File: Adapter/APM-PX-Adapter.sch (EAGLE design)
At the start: 13 parts, among them Q1 BSS138, Q2 BSS138

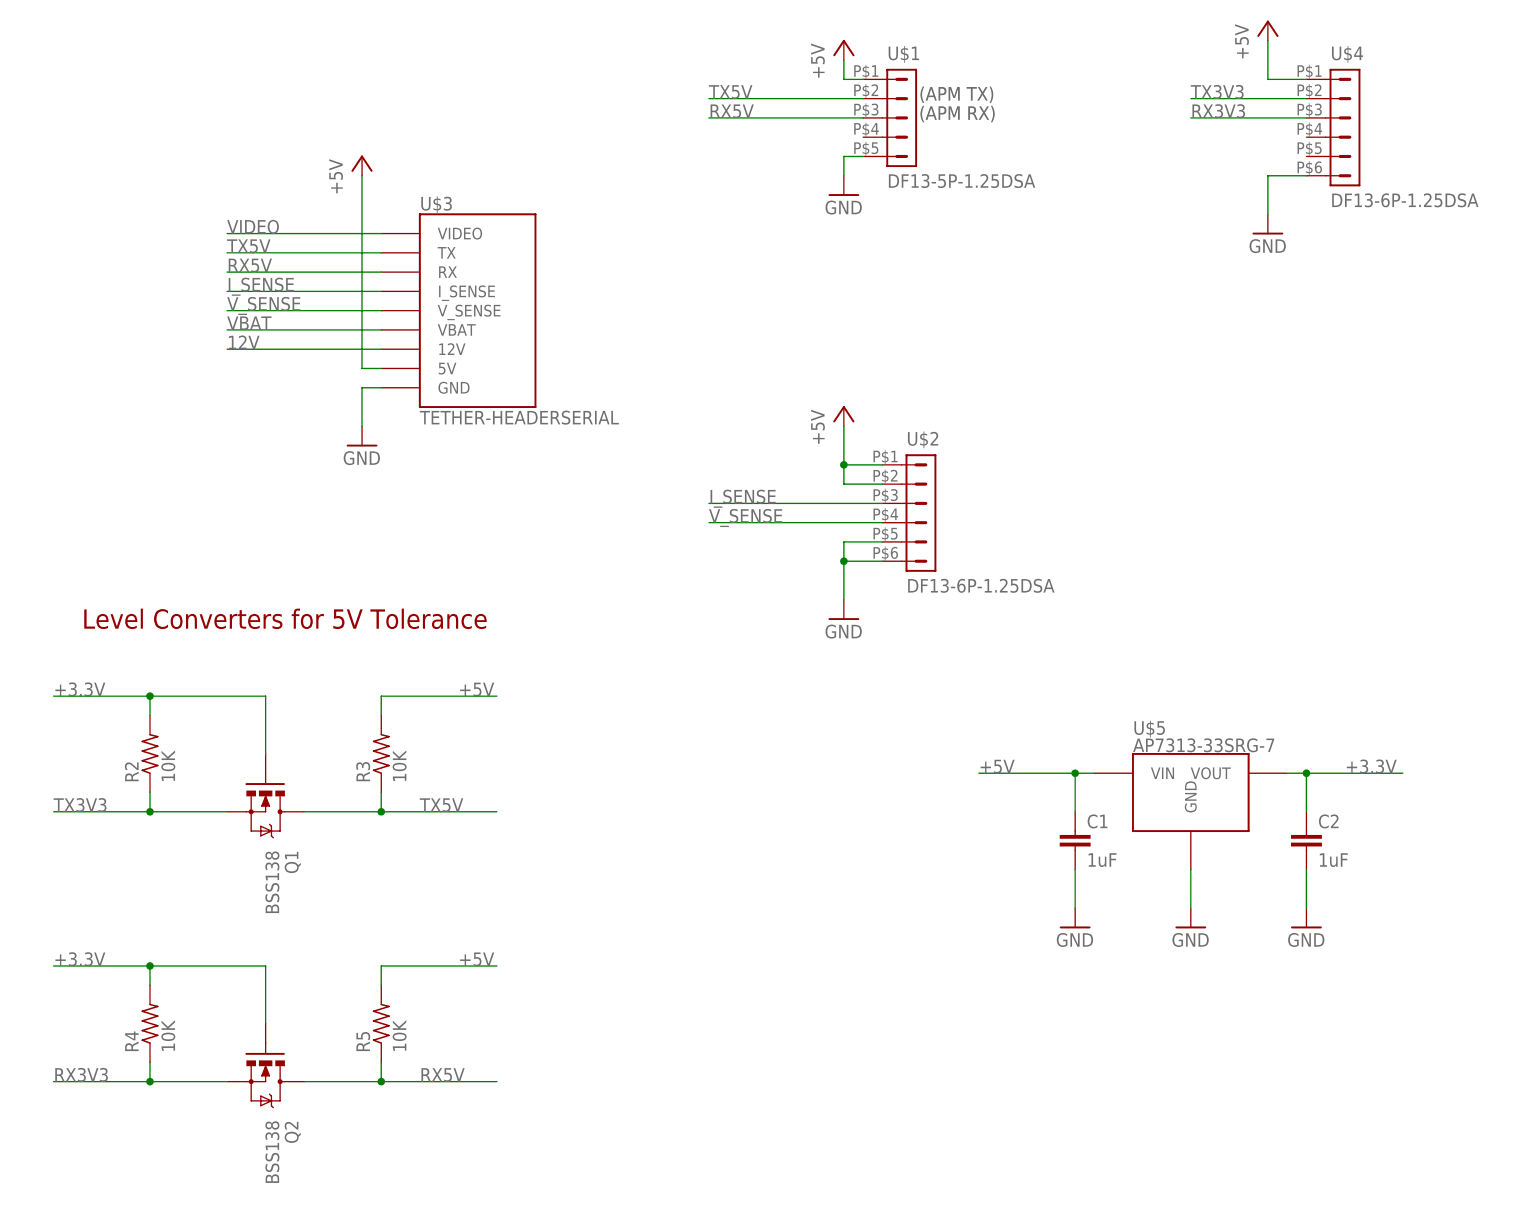
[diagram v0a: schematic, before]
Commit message: Removed level shifting and switch to all through hole components. Ordering a prototype.
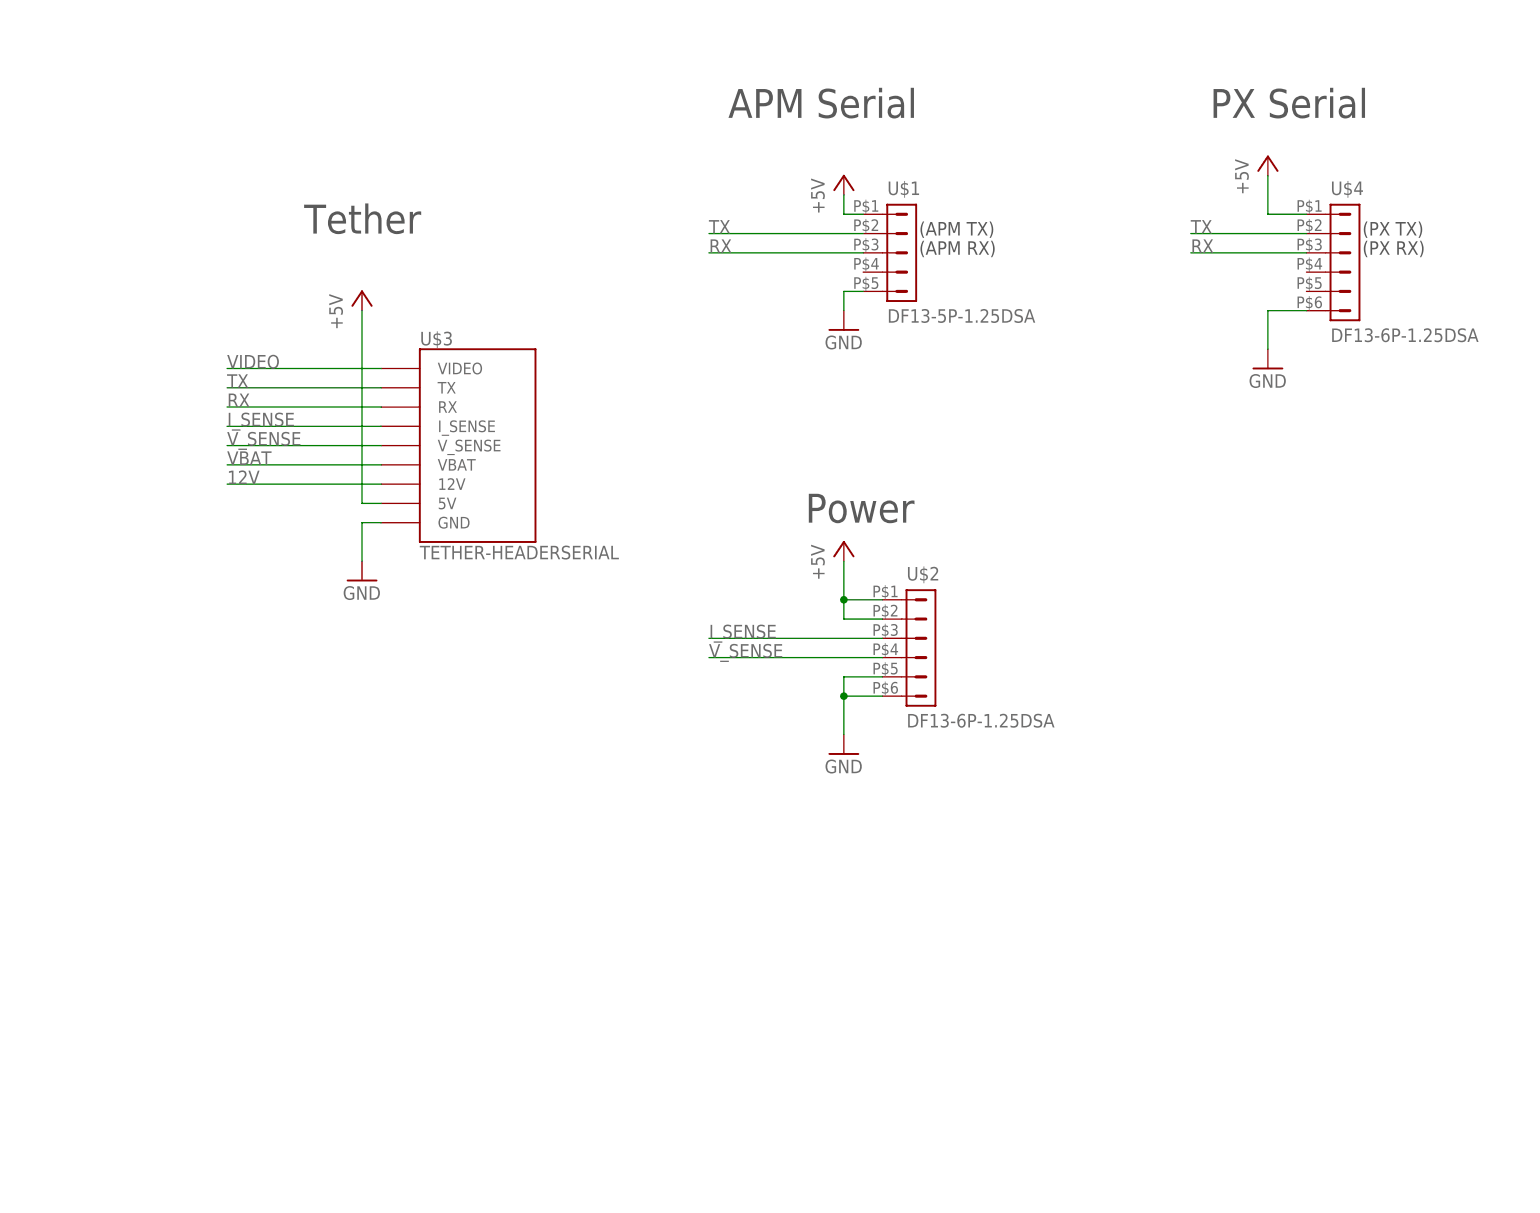
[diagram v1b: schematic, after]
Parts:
- removed C1, C2: 1uF, resistor:C-EUC0603
- removed Q1, Q2: BSS138, SparkFun-DiscreteSemi:MOSFET-NCHANNEL2N7002PW
- removed R2, R3, R4, R5: 10K, resistor:R-US_R0402
- removed U$5: AP7313-33SRG-7, BlueRobotics-Main:VREG-ZXTR2105
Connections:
- removed net +3.3V: C2.1, Q1.G, Q2.G, R2.2, R4.2, U$5.VOUT
- removed net RX3V3: Q2.S, R4.1, U$4.3
- removed net RX5V: Q2.D, R5.1, U$1.3, U$3.RX
- removed net TX3V3: Q1.S, R2.1, U$4.2
- removed net TX5V: Q1.D, R3.1, U$1.2, U$3.TX
- new net RX: U$1.3, U$3.RX, U$4.3
- new net TX: U$1.2, U$3.TX, U$4.2
- net +5V: no longer C1.1, R3.2, R5.2, U$5.VIN
- net GND: no longer C1.2, C2.2, U$5.GND
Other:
- note added: "(PX RX)"
- note added: "(PX TX)"
- note added: "APM Serial"
- note added: "PX Serial"
- note added: "Power"
- note added: "Tether"
- note removed: "Level Converters for 5V Tolerance"
- moved on the sheet: U$1, U$2, U$3, U$4

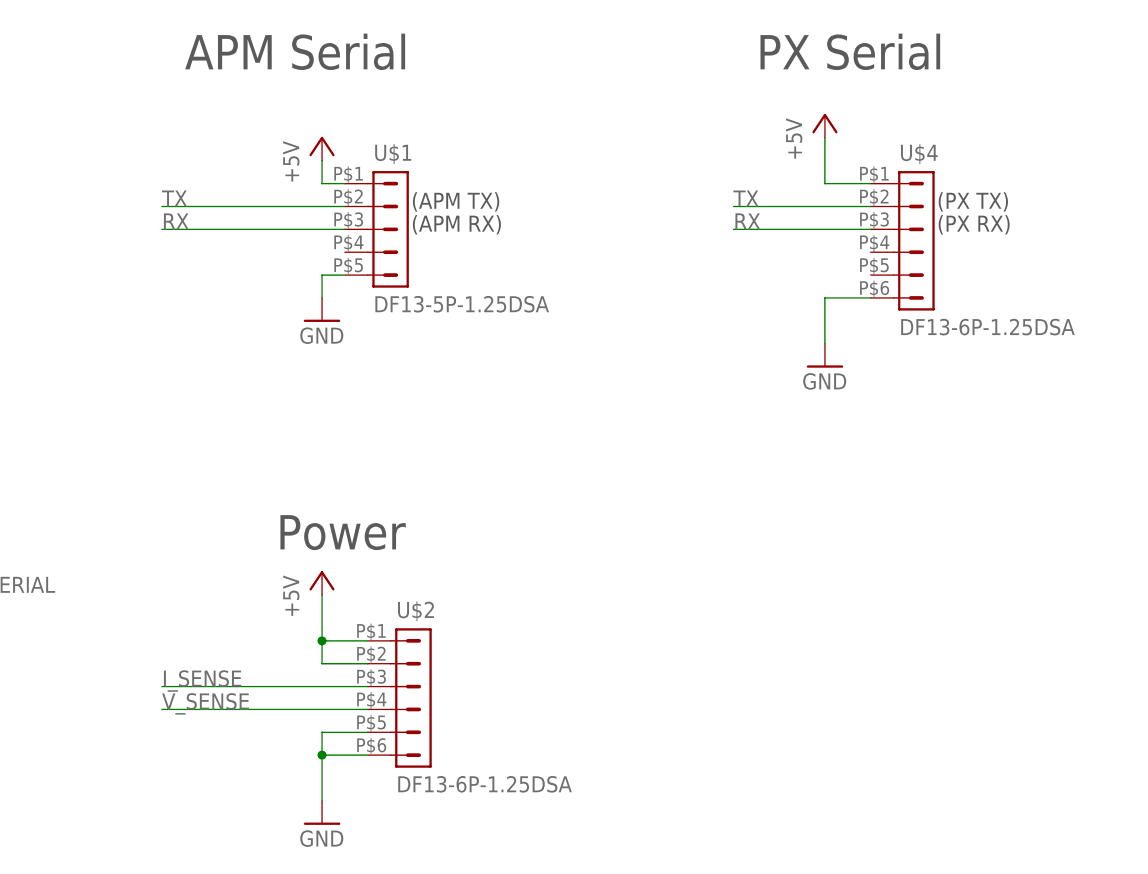
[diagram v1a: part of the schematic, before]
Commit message: Updates to adapter board.
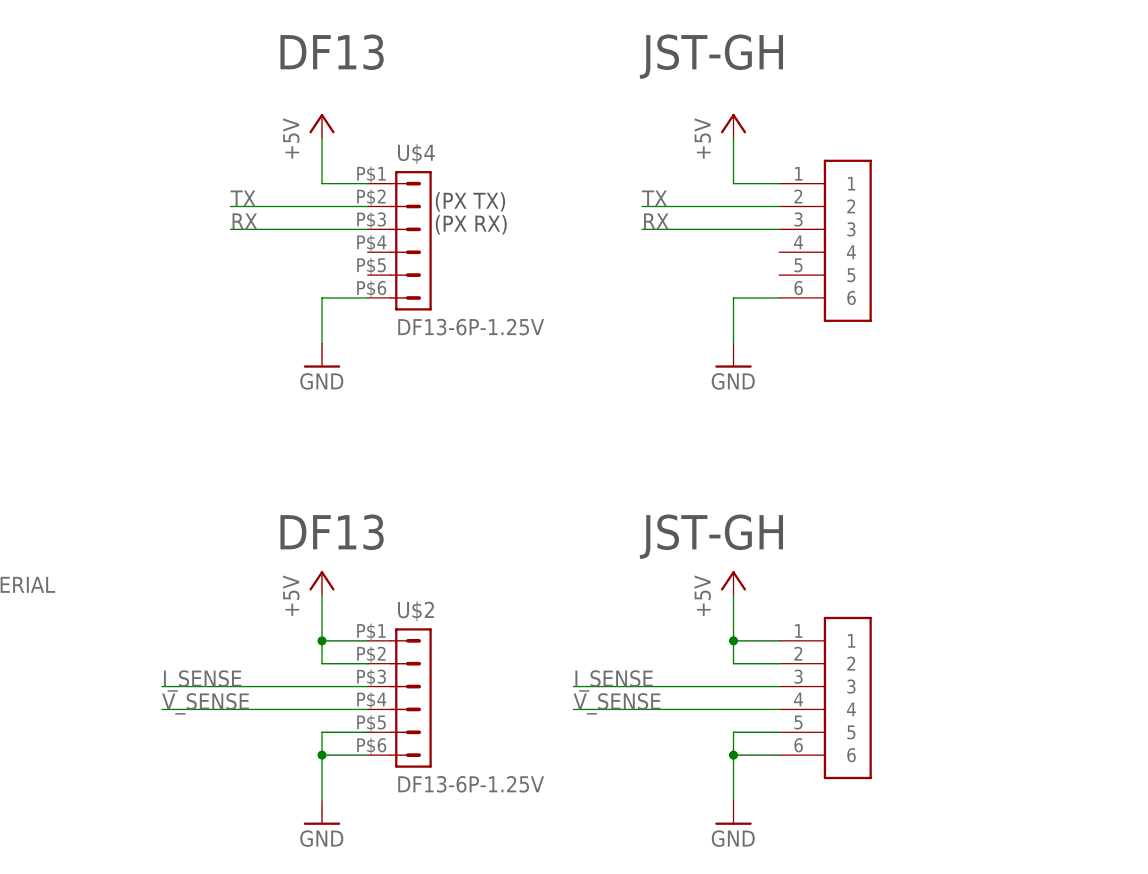
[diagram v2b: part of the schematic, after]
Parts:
- added U$5: JST-GH-6TOP-ENTRY, BlueRobotics-JST-GH:JST-GH-6TOP-ENTRY
- U$1: value DF13-5P-1.25DSA -> JST-GH-6TOP-ENTRY; device con-hirose-df13:DF13-5P-1.25DSA -> BlueRobotics-JST-GH:JST-GH-6TOP-ENTRY
- U$2, U$4: value DF13-6P-1.25DSA -> DF13-6P-1.25V; device con-hirose-df13:DF13-6P-1.25DSA -> con-hirose-df13:DF13-6P-1.25V
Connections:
- net +5V: now also U$5.1, U$5.2
- net GND: now also U$1.6, U$5.5, U$5.6; no longer U$1.5
- net I_SENSE: now also U$5.3
- net V_SENSE: now also U$5.4
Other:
- note added: "DF13"
- note added: "JST-GH"
- note removed: "(APM RX)"
- note removed: "(APM TX)"
- note removed: "APM Serial"
- note removed: "PX Serial"
- note removed: "Power"
- moved on the sheet: U$4
